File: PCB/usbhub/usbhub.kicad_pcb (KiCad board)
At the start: 2 copper layers, 30.7 x 55 mm, 37 parts, among them U1 SL2.1S, U2 SL2.1S

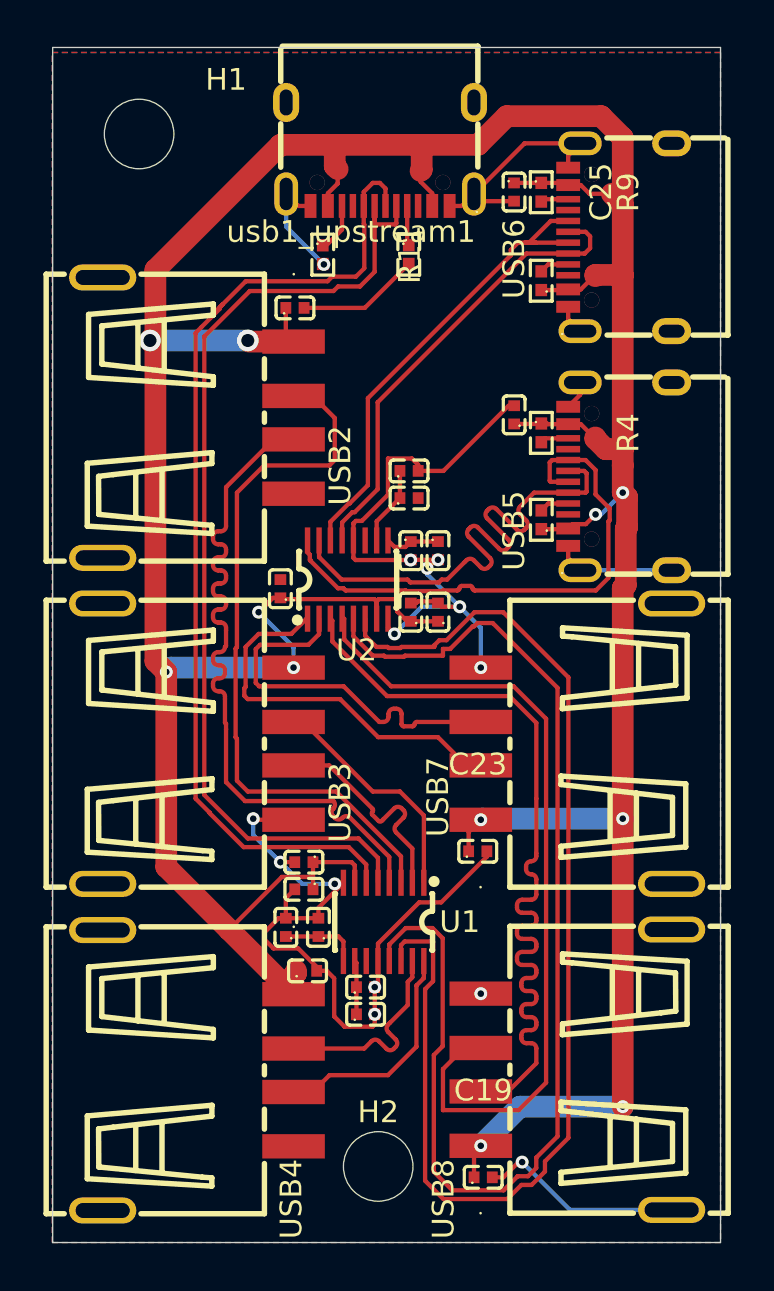
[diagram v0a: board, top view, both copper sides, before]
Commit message: tune skew, eliminate via-in-pad, improve gnd connections
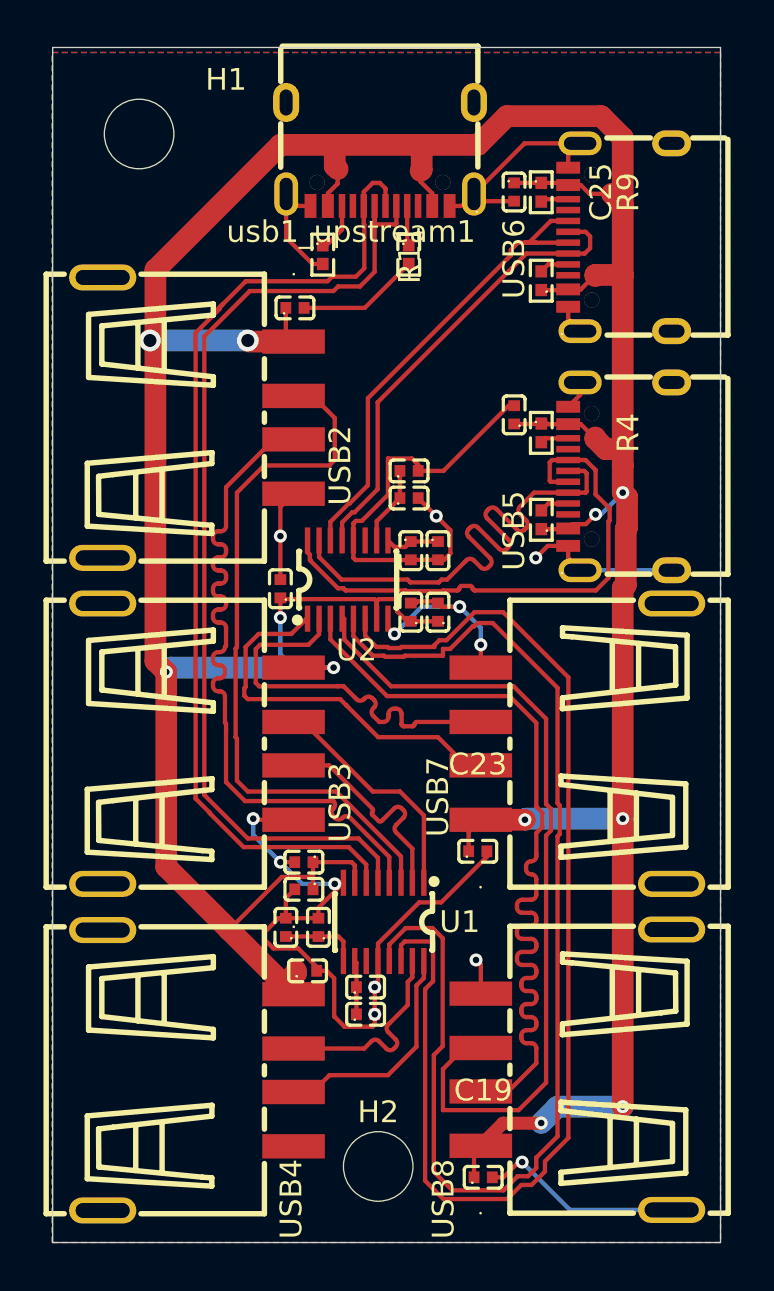
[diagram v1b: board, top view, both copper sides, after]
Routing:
- net GND: track 101.3 -> 110.0 mm, vias 14 -> 13
- net /VBUS: track 185.5 -> 188.7 mm
- net /D2B+: track 16.5 -> 17.1 mm

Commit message: nit
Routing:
- net GND: track 110.0 -> 112.3 mm
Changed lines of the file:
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@@
+	)
+	(segment
+		(start 171.32 65.57)
+		(end 170.75 65)
+		(width 0.2)
+		(layer "F.Cu")
+		(net "GND")
 	)
 	(segment
@@
 		(width 0.2)
 		(layer "F.Cu")
+		(net "GND")
+	)
+	(segment
+		(start 172.79 65.57)
+		(end 171.32 65.57)
+		(width 0.2)
+		(layer "F.Cu")

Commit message: final
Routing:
- net /D1A+: track 31.7 -> 27.4 mm
- net /D2A+: track 10.5 -> 8.62 mm
- net /D2B+: track 17.1 -> 15.3 mm
- net /D2A-: track 10.4 -> 9.70 mm
